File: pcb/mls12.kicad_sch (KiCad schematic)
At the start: 0 parts

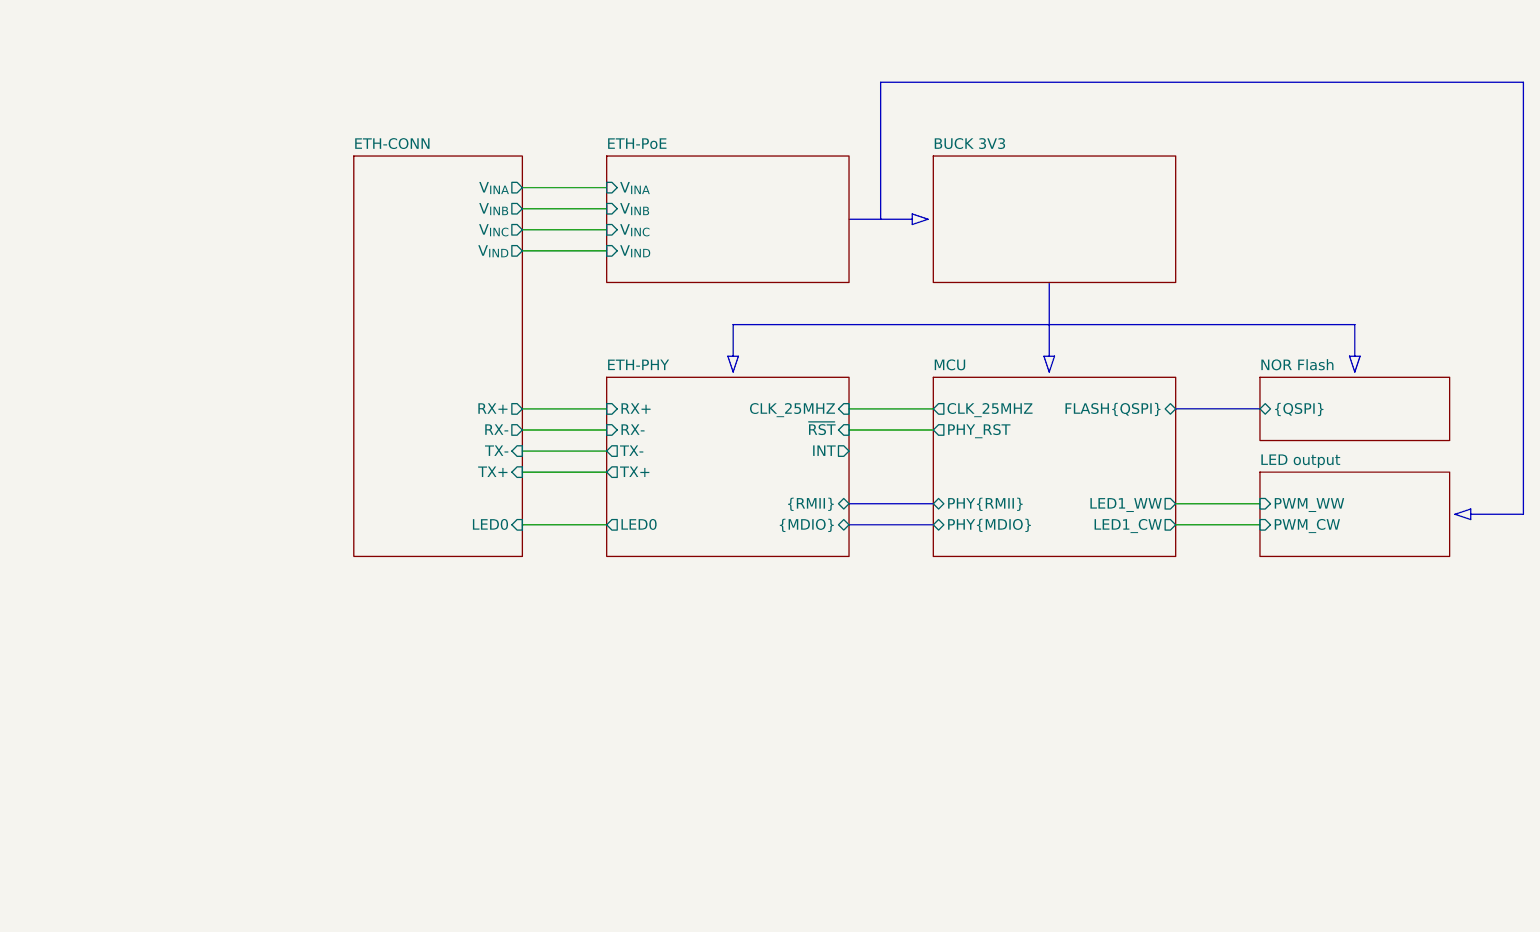
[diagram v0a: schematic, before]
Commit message: Update to 25W PoE+ module, 2 outputs
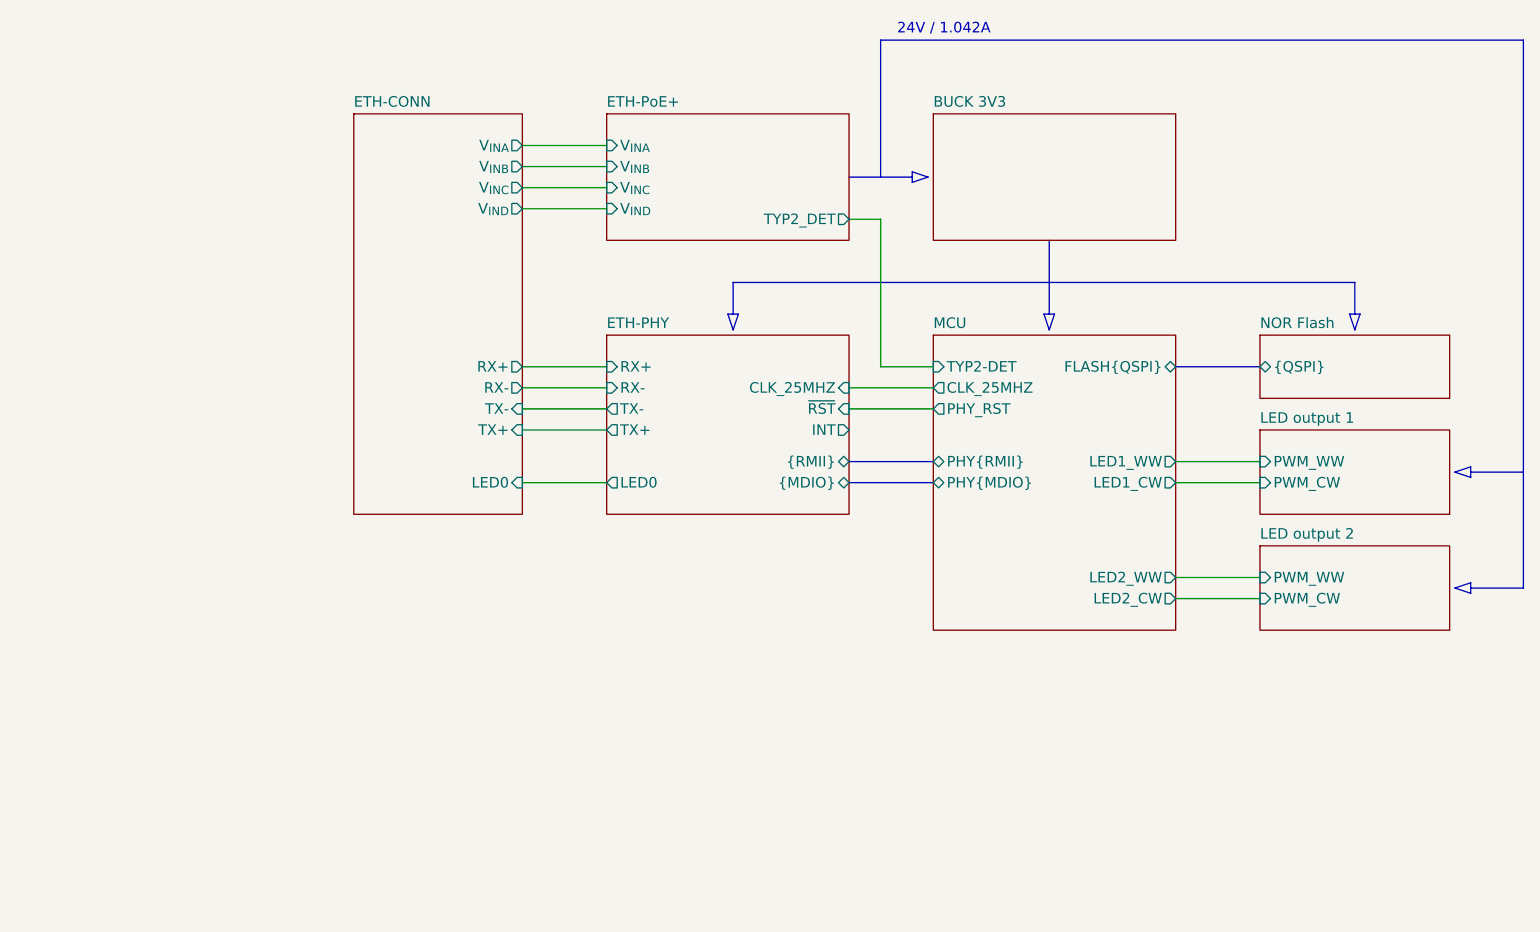
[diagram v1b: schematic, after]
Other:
- sheet ETH-PoE renamed ETH-PoE+
- sheet LED output renamed LED output 1
- added sheet LED output 2 (mls12_led_output.kicad_sch)
- sheet ETH-PoE+ ports: added TYP2_DET; removed none
- sheet MCU ports: added LED2_CW, LED2_WW, TYP2-DET; removed none
- note added: "24V / 1.042A"
- title: MLS12 — PoE LED driver -> MLS25 — PoE+ LED driver

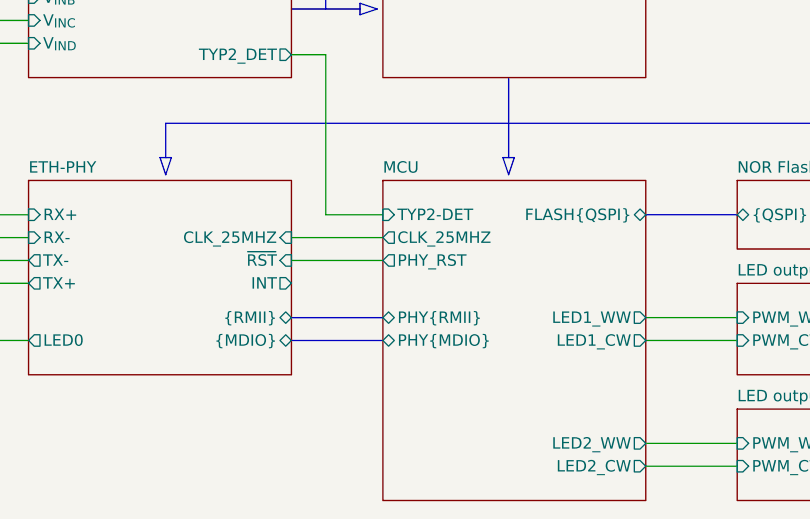
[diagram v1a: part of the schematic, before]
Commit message: Route PHY IRQ
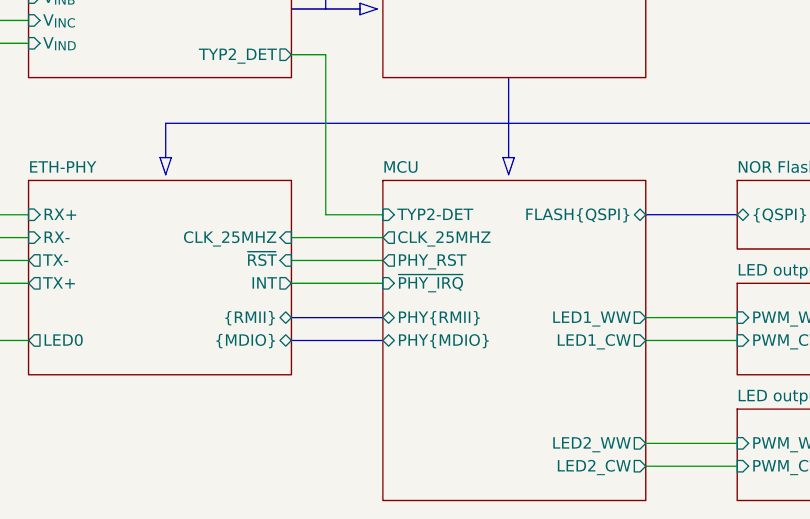
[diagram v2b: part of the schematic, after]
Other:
- sheet MCU ports: added ~{PHY_IRQ}; removed none
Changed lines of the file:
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@@
+		)
+	)
+	(wire
+		(pts
+			(xy 138.43 109.22) (xy 148.59 109.22)
+		)
+		(stroke
+			(width 0)
+			(type default)
 		)
 	)
@@
 			)
 		)
+		(pin "~{PHY_IRQ}" input
+			(at 148.59 109.22 180)
+			(effects
+				(font
+					(size 1.27 1.27)
+				)
+				(justify left)
+			)
+		)

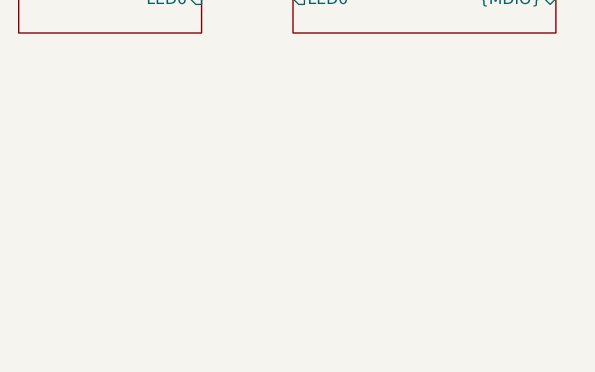
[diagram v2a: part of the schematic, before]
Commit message: Add mounting holes, round corners
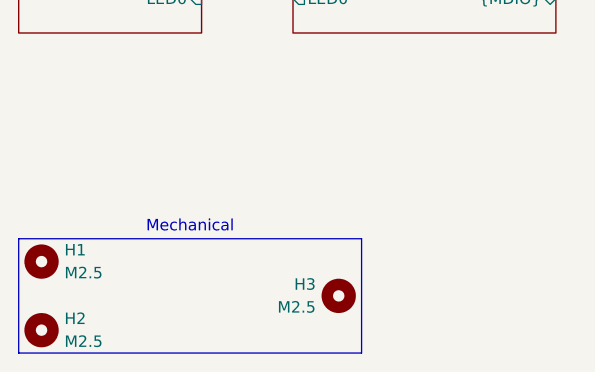
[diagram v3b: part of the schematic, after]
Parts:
- added H1, H2, H3: M2.5, MountingHole:MountingHole_2.7mm_M2.5_ISO7380, symbol Mechanical:MountingHole
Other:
- note added: "Mechanical"

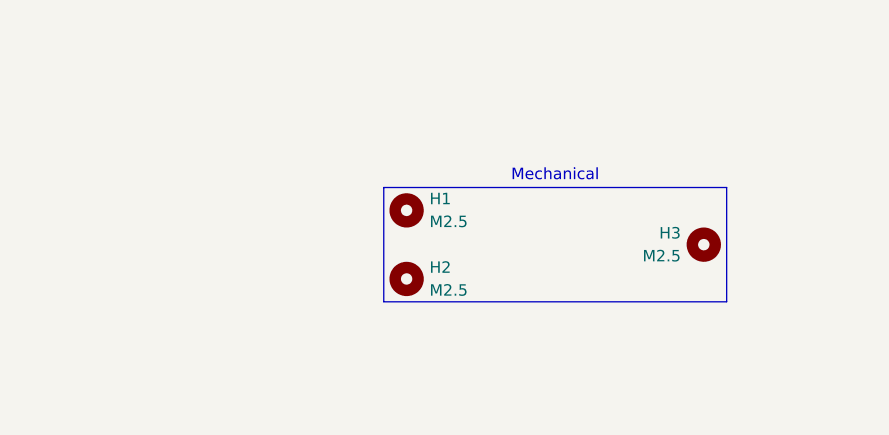
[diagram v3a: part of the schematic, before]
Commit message: Add power planes, fiducials
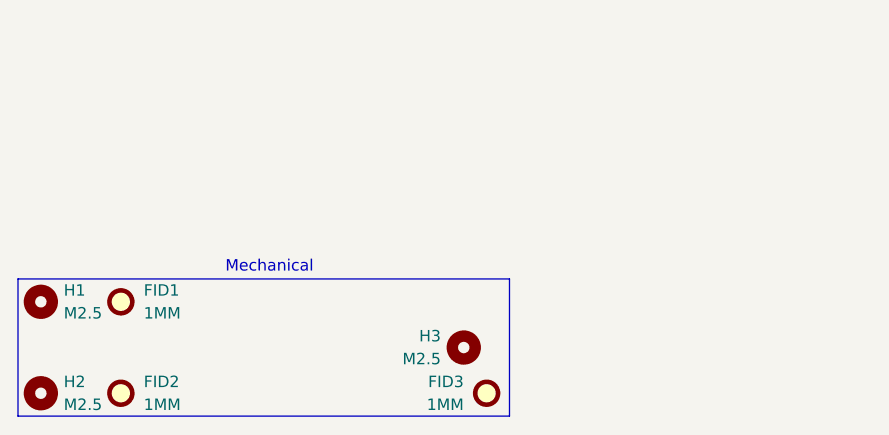
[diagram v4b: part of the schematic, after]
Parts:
- added FID1, FID2, FID3: 1MM, Fiducial:Fiducial_1mm_Mask2mm, symbol Mechanical:Fiducial
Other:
- moved on the sheet: H1, H2, H3
